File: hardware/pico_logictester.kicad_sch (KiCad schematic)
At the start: 29 parts, among them J1 Conn_02x09_Odd_Even, J2 GPIO_5_28, J3 AKKU, J4 STEP_UP_IN, J5 5V VERSORGUNG, J6 TFT Display, Q1 AO3401A, Q2 BC547, SW1 SW_Push, U1 74HC245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

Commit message: doc: Schaltplan v1.0 als PDF hinzugefügt
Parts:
- SW1: footprint Button_Switch_THT:SW_PUSH_6mm_H9.5mm -> Button_Switch_THT:SW_Tactile_SPST_Angled_PTS645Vx83-2LFS
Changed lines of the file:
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@@
 			)
 		)
-		(property "Footprint" "Button_Switch_THT:SW_PUSH_6mm_H9.5mm"
+		(property "Footprint" "Button_Switch_THT:SW_Tactile_SPST_Angled_PTS645Vx83-2LFS"
 			(at 121.92 179.07 0)
 			(effects

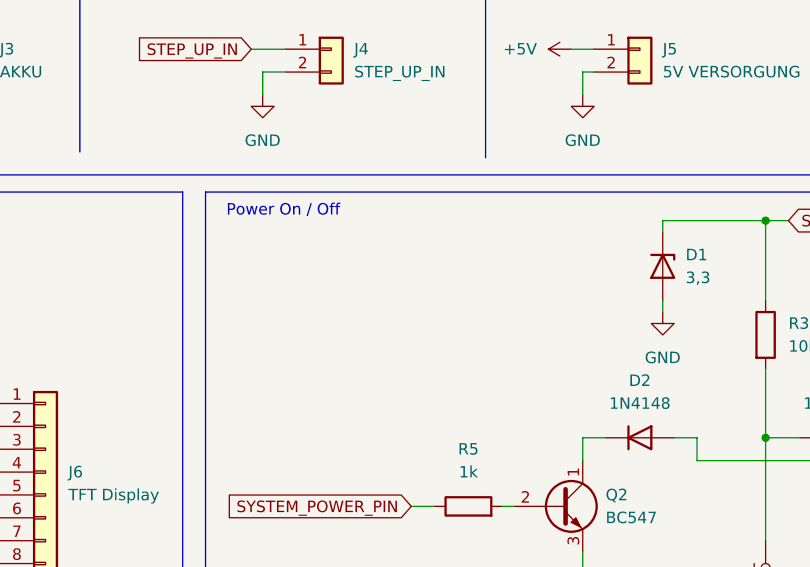
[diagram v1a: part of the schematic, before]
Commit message: Hinweis im Schaltplan hinzugefügt. D2 kann entfallen, und wird nicht benötigt.
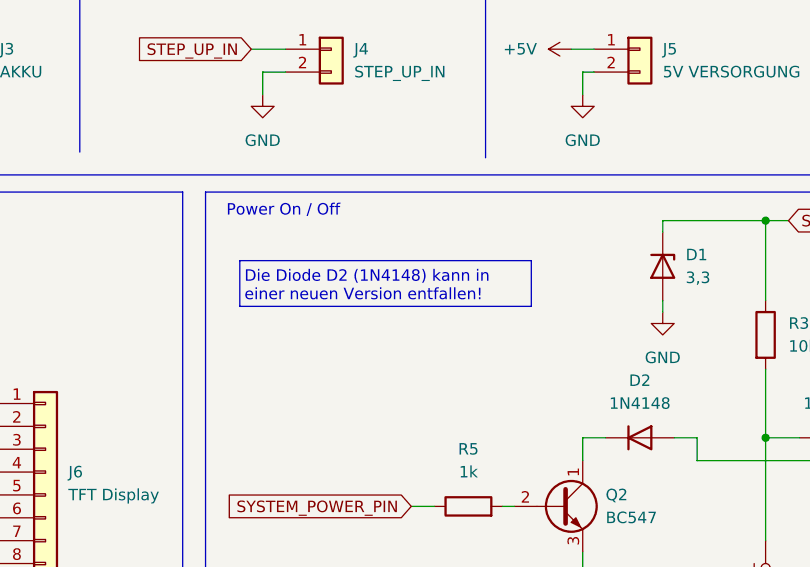
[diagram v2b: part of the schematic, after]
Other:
- note added: "Die Diode D2 (1N4148) kann in einer neuen Version entfallen!"
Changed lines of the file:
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@@
+		)
+	)
+	(rectangle
+		(start 68.58 142.875)
+		(end 100.965 147.955)
+		(stroke
+			(width 0)
+			(type default)
+		)
+		(fill
+			(type none)
 		)
 	)
@@
 		)
 	)
+	(text "Die Diode D2 (1N4148) kann in \neiner neuen Version entfallen!"
+		(exclude_from_sim no)
+		(at 69.088 145.796 0)
+		(effects
+			(font
+				(size 1.27 1.27)
+			)
+			(justify left)
+		)
+	)
